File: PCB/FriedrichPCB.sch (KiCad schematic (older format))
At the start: 122 parts, among them U1 ATmega32U4-AU, U2 SRV05-4, X1 Crystal_GND24_Small

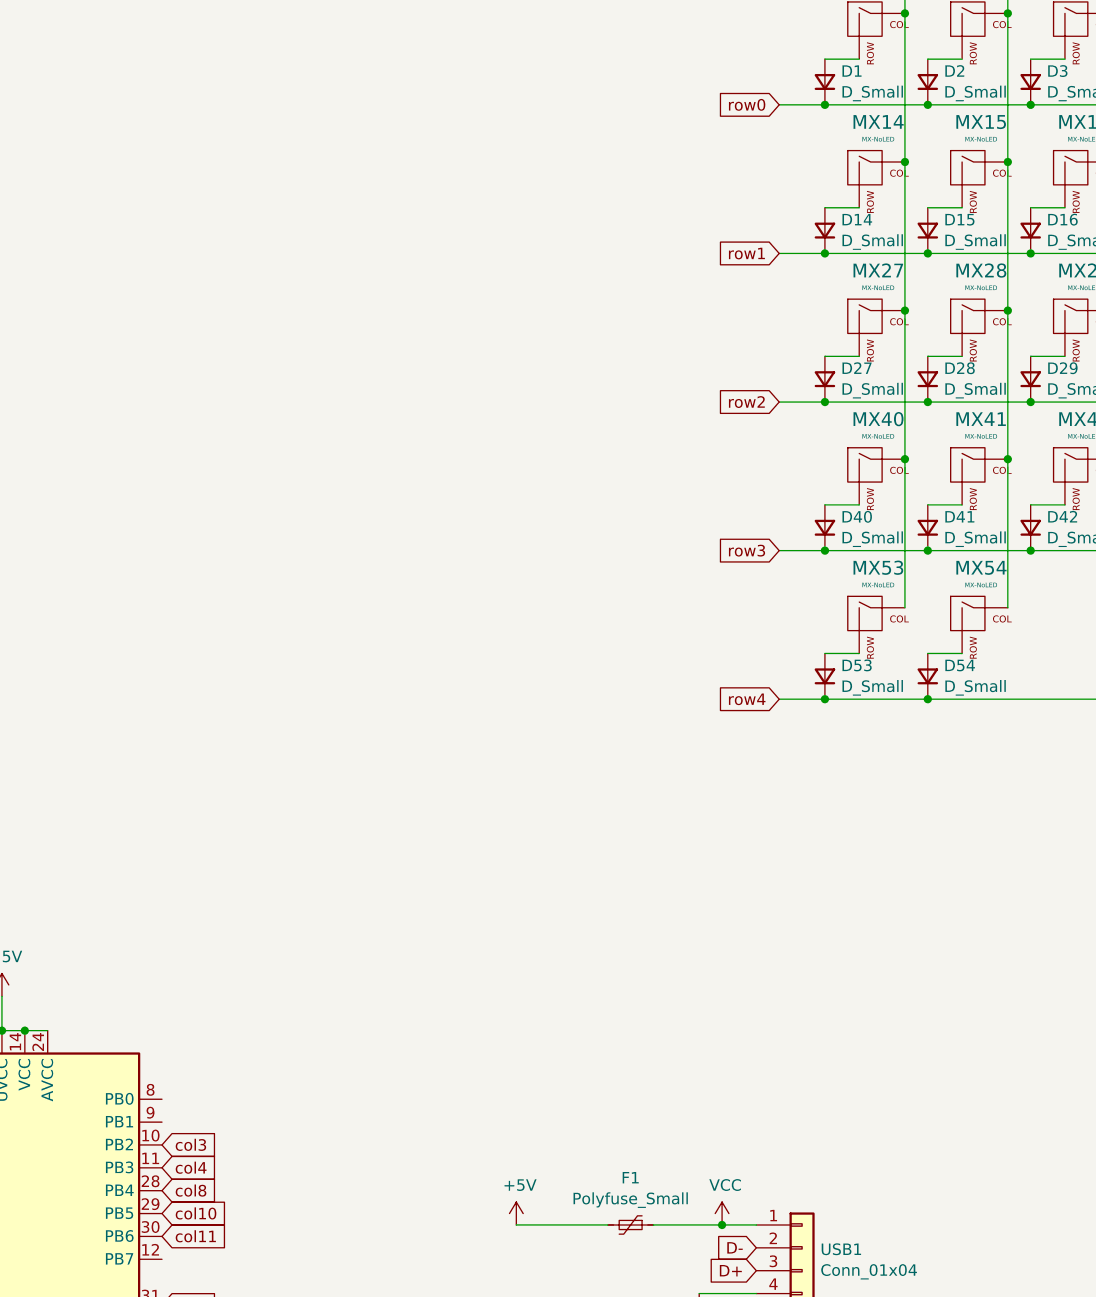
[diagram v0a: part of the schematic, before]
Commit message: add Capslock LED
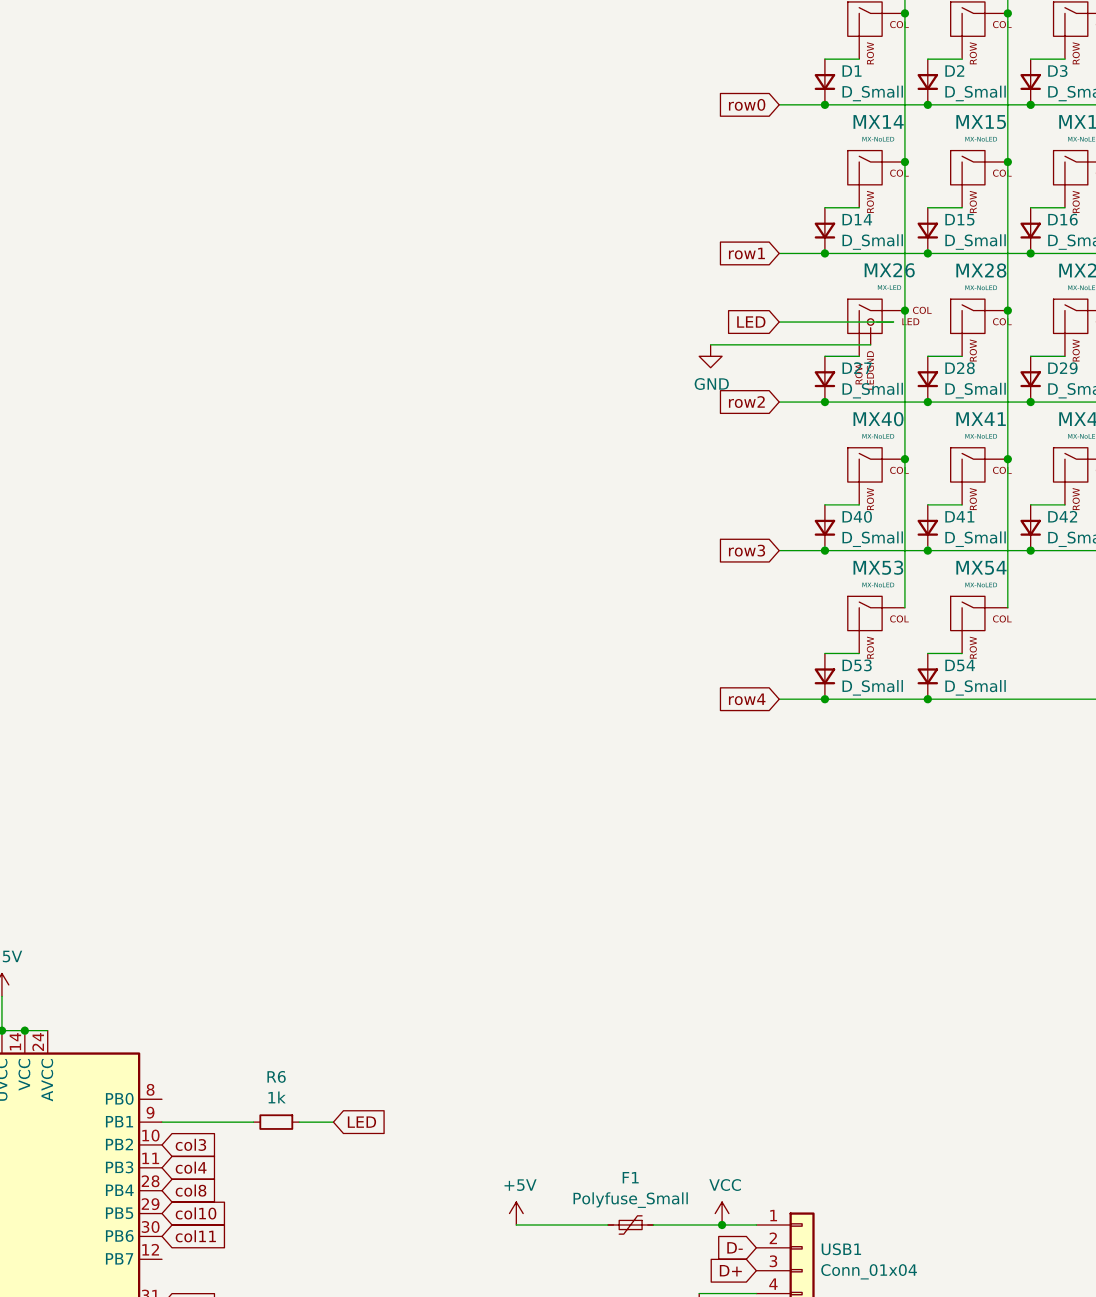
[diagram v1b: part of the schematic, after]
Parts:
- removed MX27: MX-NoLED, MX_Only:MXOnly-1.75U-NoLED, symbol MX_Alps_Hybrid:MX-NoLED
- added MX26: MX-LED, MX_Only:MXOnly-1.75U, symbol MX_Alps_Hybrid:MX-LED
- added R6: 1k, Resistor_SMD:R_0805_2012Metric, symbol Device:R_Small
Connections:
- net GND: now also MX26.4 (LEDGND)
- net col0: now also MX26.1 (COL)
- net at U1.9 (PB1): now also R6.2
- net at D27.2 (A): now also MX26.2 (ROW)
- new net LED: MX26.3 (LED), R6.1
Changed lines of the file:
@@
 	11800 3450 11650 3450
-$Comp
-L MX_Alps_Hybrid:MX-NoLED MX27
-U 1 1 601F5D26
-P 6900 3950
-F 0 "MX27" H 6933 4173 60  0000 C CNN
-F 1 "MX-NoLED" H 6933 4099 20  0000 C CNN
-F 2 "MX_Only:MXOnly-1.75U-NoLED" H 6275 3925 60  0001 C CNN
-F 3 "" H 6275 3925 60  0001 C CNN
-	1    6900 3950
-	1    0    0    -1
-$EndComp
 $Comp
 L Device:D_Small D27
@@
 Wire Wire Line
 	7050 3250 7050 2600
-Connection ~ 7050 3900
-Wire Wire Line
-	7050 3900 7050 3250
 Connection ~ 7050 4550
-Wire Wire Line
-	7050 4550 7050 3900
 Wire Wire Line
 	10750 4950 11650 4950
@@
 Text GLabel 3800 9050 2    50   Input ~ 0
 row4
+Text GLabel 6500 3950 0    50   Input ~ 0
+LED
+Connection ~ 7050 3900
+Wire Wire Line
+	7050 3250 7050 3900
+Wire Wire Line
+	7050 3900 7050 4550
+$Comp
+L MX_Alps_Hybrid:MX-LED MX26
+U 1 1 601225BC
+P 6900 3950
+F 0 "MX26" H 6982 4174 60  0000 C CNN
+F 1 "MX-LED" H 6982 4100 20  0000 C CNN
+F 2 "MX_Only:MXOnly-1.75U" H 6275 3925 60  0001 C CNN
+F 3 "" H 6275 3925 60  0001 C CNN
+	1    6900 3950
+	1    0    0    -1
+$EndComp
+Wire Wire Line
+	7000 3950 6500 3950
+$Comp
+L power:GND #PWR0101
+U 1 1 6013C58E
+P 6200 4050
+F 0 "#PWR0101" H 6200 3800 50  0001 C CNN
+F 1 "GND" H 6205 3877 50  0000 C CNN
+F 2 "" H 6200 4050 50  0001 C CNN
+F 3 "" H 6200 4050 50  0001 C CNN
+	1    6200 4050
+	1    0    0    -1
+$EndComp
+Wire Wire Line
+	6200 4050 6900 4050
+$Comp
+L Device:R_Small R6
+U 1 1 6014A442
+P 4300 7450
+F 0 "R6" V 4104 7450 50  0000 C CNN
+F 1 "1k" V 4195 7450 50  0000 C CNN
+F 2 "Resistor_SMD:R_0805_2012Metric" H 4300 7450 50  0001 C CNN
+F 3 "~" H 4300 7450 50  0001 C CNN
+F 4 "C17414" V 4300 7450 50  0001 C CNN "LCSC"
+	1    4300 7450
+	0    1    1    0
+$EndComp
+Wire Wire Line
+	3800 7450 4200 7450
+Text GLabel 4550 7450 2    50   Input ~ 0
+LED
+Wire Wire Line
+	4400 7450 4550 7450
 $EndSCHEMATC
